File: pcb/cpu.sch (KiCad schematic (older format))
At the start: 37 parts, among them P2 BATT1, P27 BDM, P57 TX1, P58 RX1, P59 TX, P60 RX, P64 RXCAN0, P65 TXCAN0, U1 MC9S12XDP512, U5 M41T56M6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

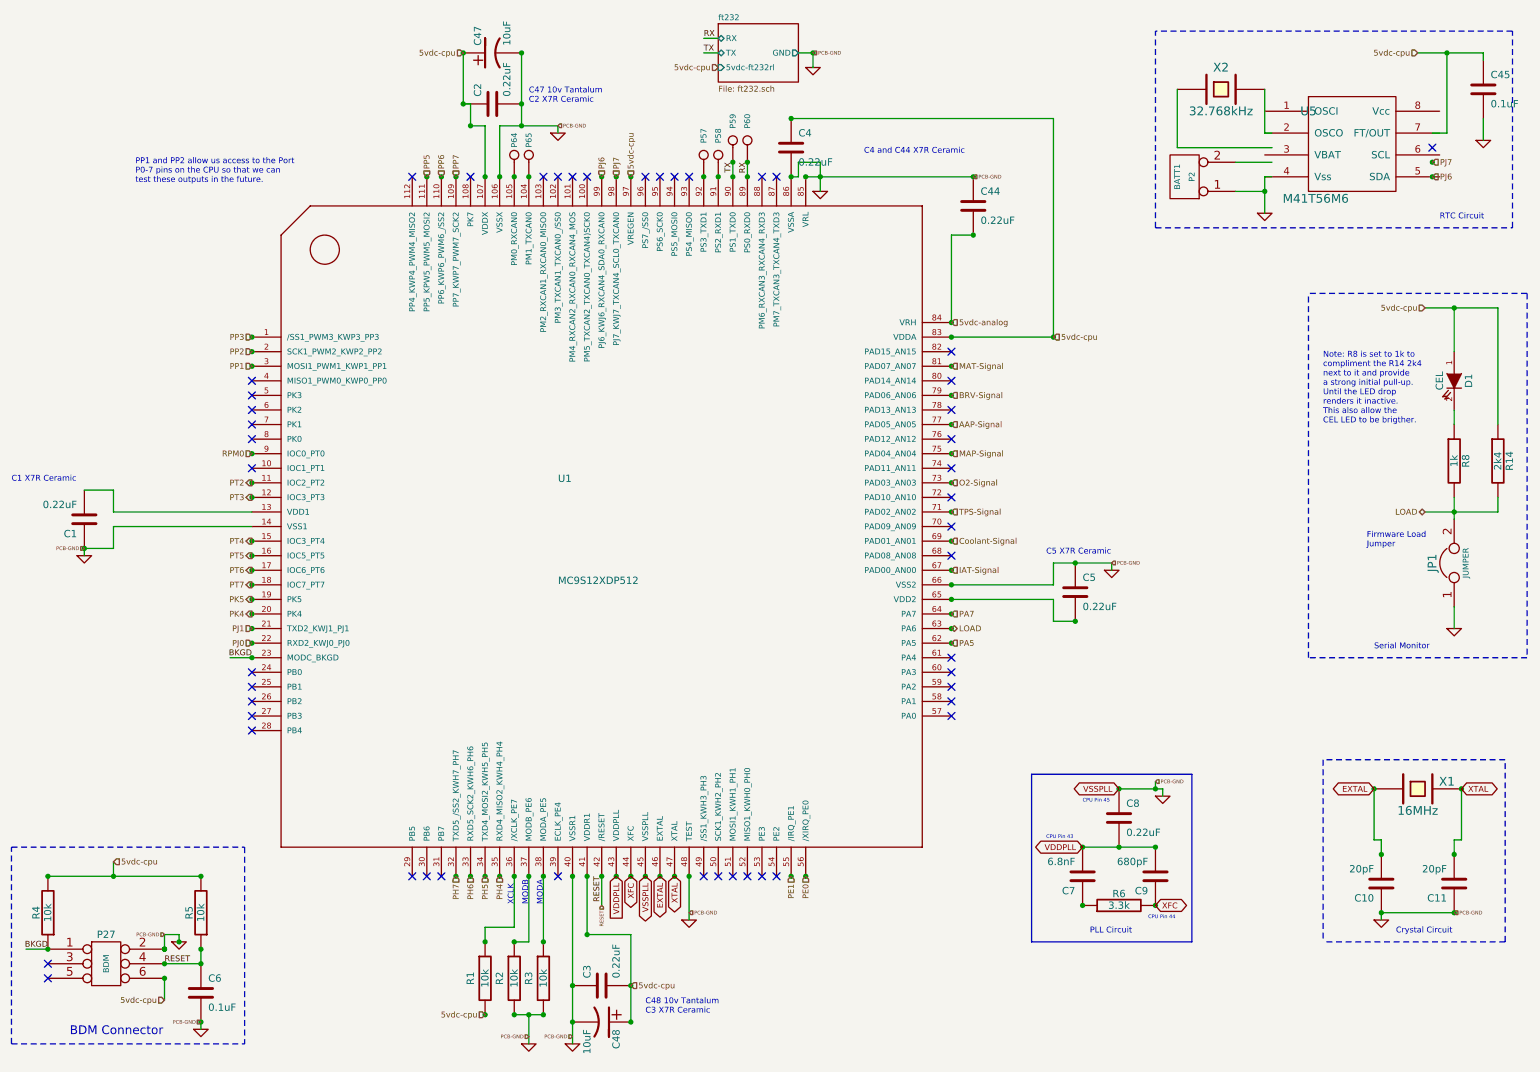
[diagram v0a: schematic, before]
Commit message: Change CEL/Load Circuit (add a R10 1k resistor)
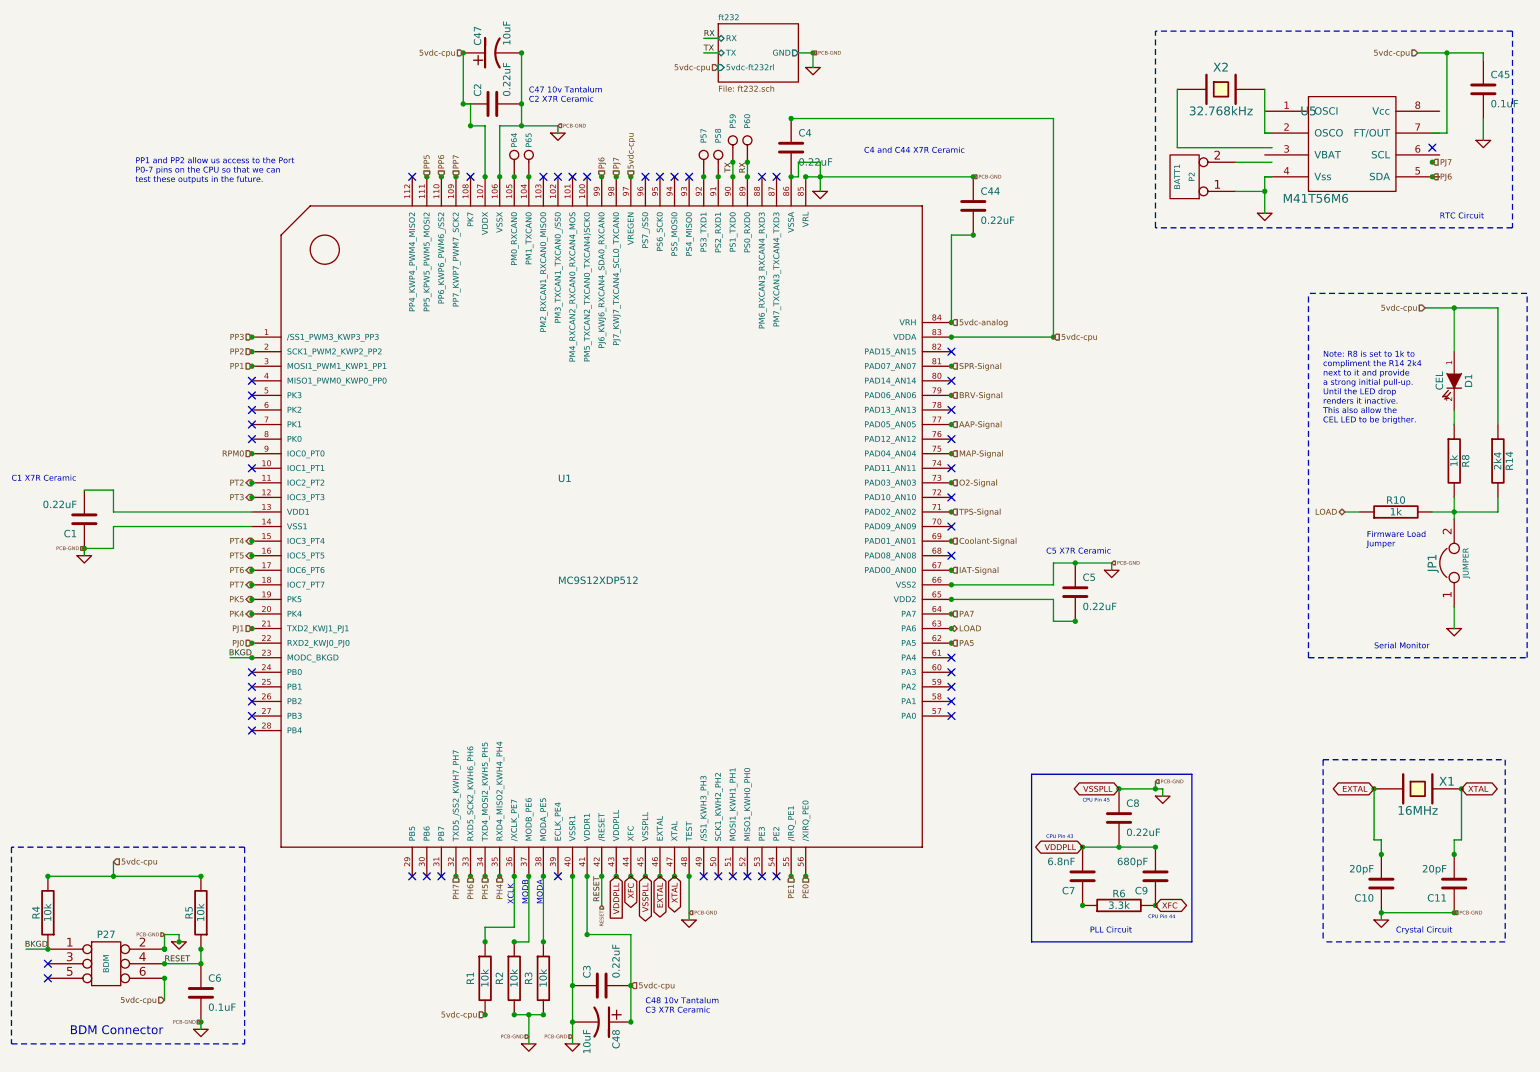
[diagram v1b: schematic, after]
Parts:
- added R10: 1k, symbol R
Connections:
- net labels added: SPR-Signal
- net labels removed: MAT-Signal
- wire segments 97 -> 98

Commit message: schematics update
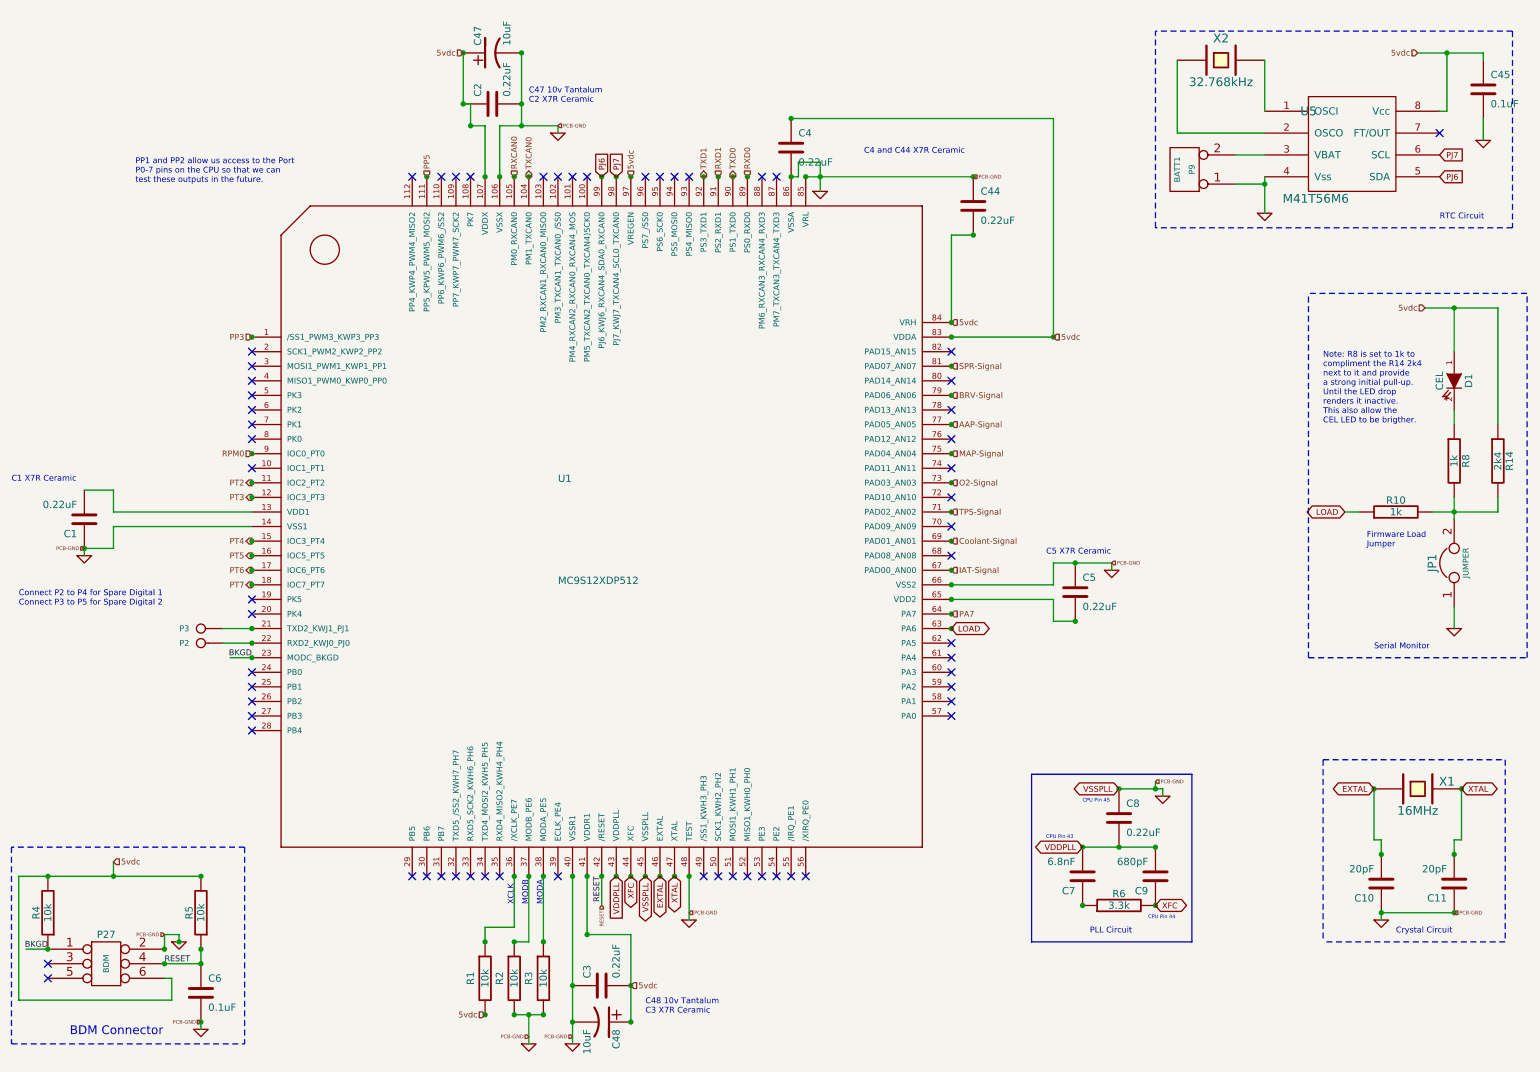
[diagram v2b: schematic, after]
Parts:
- removed P57: TX1, symbol CONN_1
- removed P58: RX1, symbol CONN_1
- removed P59: TX, symbol CONN_1
- removed P60: RX, symbol CONN_1
- removed P64: RXCAN0, symbol CONN_1
- removed P65: TXCAN0, symbol CONN_1
- added P2, P3: CONN_1, symbol CONN_1
- renumbered P2 to P9
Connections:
- net labels added: 5vdc, RXCAN0, RXD0, RXD1, TXCAN0, TXD0, TXD1
- net labels removed: 5vdc-analog, 5vdc-cpu, PA5, PE0, PE1, PH4, PH5, PH6, PH7, PJ0, PJ1, PK4, PK5, PP1, PP2, PP6, PP7, RX, TX
- wire segments 98 -> 95
- no-connect marks 49 -> 62
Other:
- note added: "Connect P2 to P4 for Spare Digital 1\nConnect P3 to P5 for Spare Digital 2"
- moved on the sheet: P9, X2

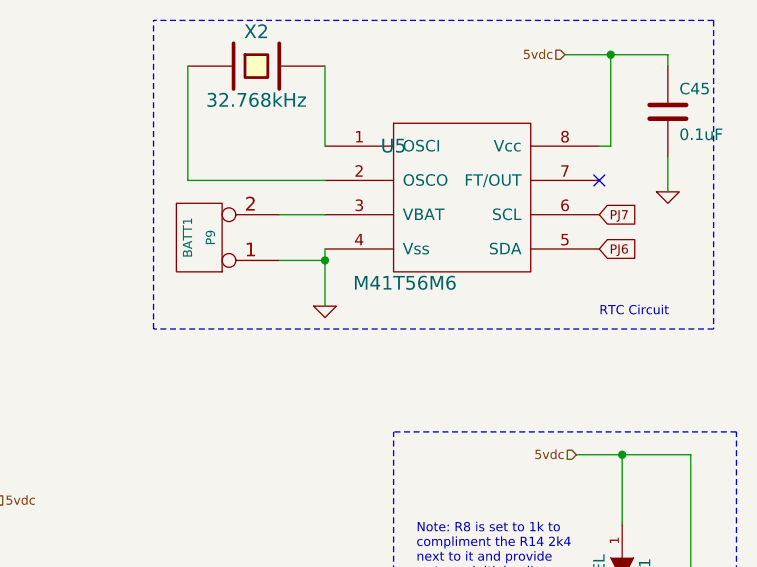
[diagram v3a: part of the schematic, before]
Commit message: replace M41T56M6 by DS1307ZN+
remove keystone103 for RTC battery and replace it by 2 pin
change MCP2551 soic8 to DIP8
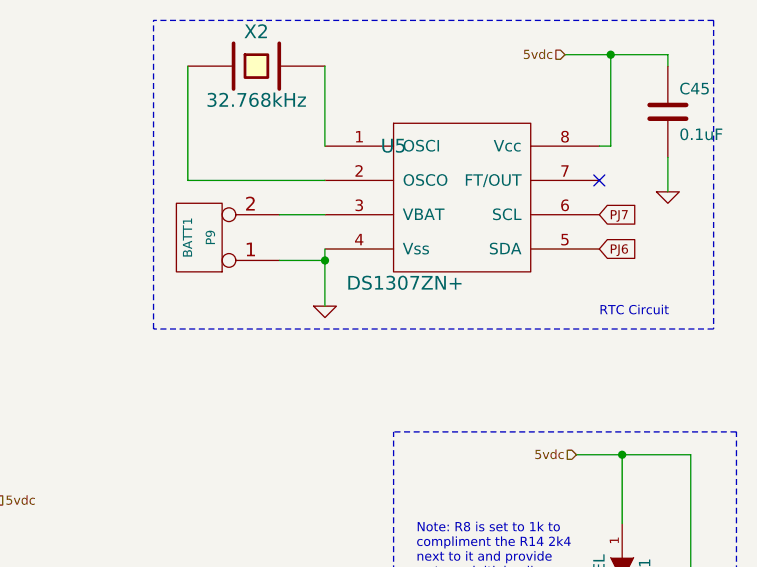
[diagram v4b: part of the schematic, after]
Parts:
- U5: value M41T56M6 -> DS1307ZN+
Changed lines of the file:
@@
-EESchema Schematic File Version 2  date 19/06/2013 13:36:51
+EESchema Schematic File Version 2  date 27/06/2013 10:27:40
 LIBS:Guepard
 LIBS:Guepard-Communication
@@
 Sheet 6 8
 Title "Guepars PCB for FreeEMS"
-Date "19 jun 2013"
+Date "27 jun 2013"
 Rev "0.1-alpha"
 Comp ""
@@
 P 9750 1600
 F 0 "U5" H 9450 1900 60  0000 C CNN
-F 1 "M41T56M6" H 9500 1300 60  0000 C CNN
+F 1 "DS1307ZN+" H 9500 1300 60  0000 C CNN
 F 2 "" H 9750 1600 60  0001 C CNN
 F 3 "" H 9750 1600 60  0001 C CNN
